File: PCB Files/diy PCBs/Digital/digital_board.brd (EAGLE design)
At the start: 50.8 x 58.4 mm, 18 parts

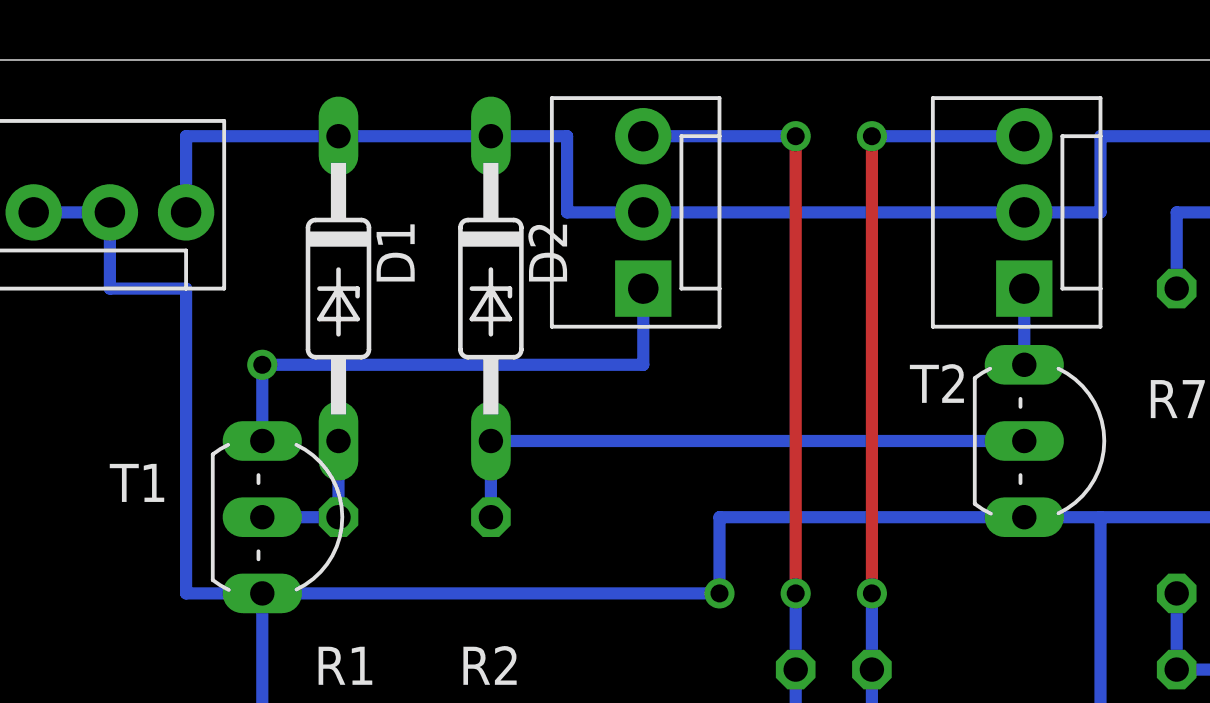
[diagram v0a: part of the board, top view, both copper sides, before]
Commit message: made fixed a small bug and changed diode parameters
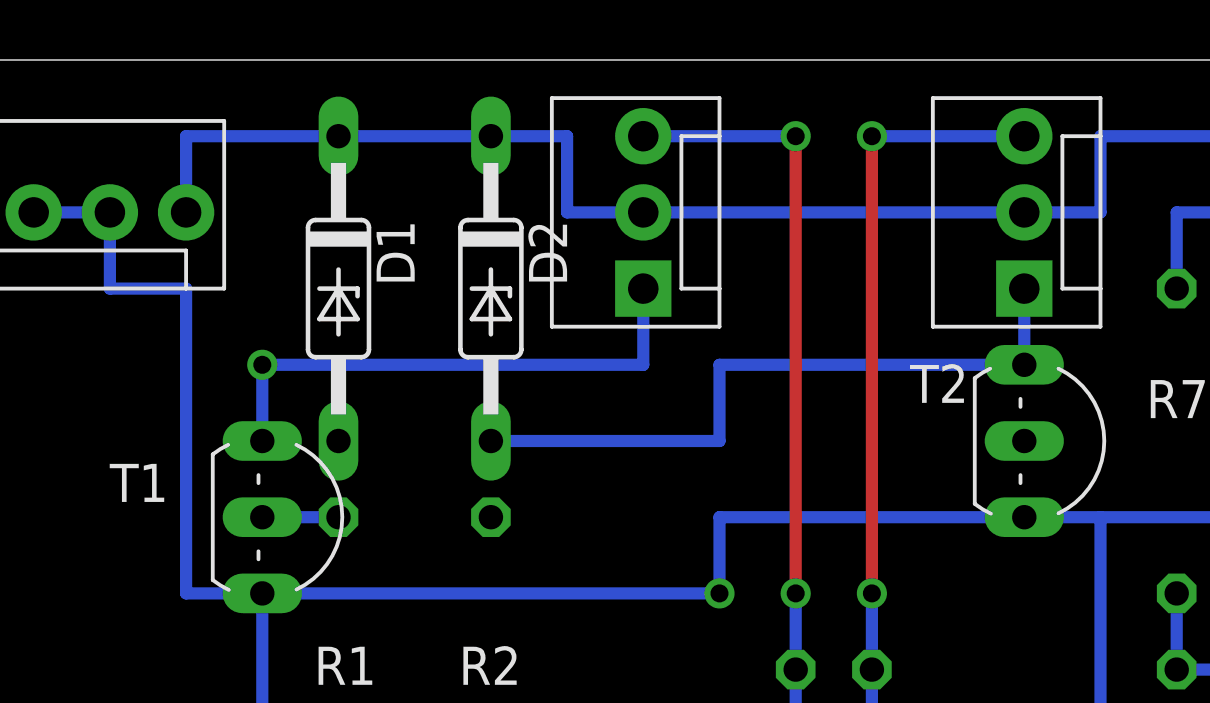
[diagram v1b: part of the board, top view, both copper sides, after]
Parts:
- D1, D2: value 1N821 -> 1N5819
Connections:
- removed net N$6: D2.A, R2.1, T2.B
- new net N$2: R2.1
- net N$3: now also D1.A
- net N$4: now also D2.A
- net N$5: no longer D1.A
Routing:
- net N$6: track 20.3 -> 0.00 mm
- net N$4: track 2.54 -> 22.9 mm
- net N$5: track 5.08 -> 2.54 mm
- net N$3: track 17.8 -> 20.3 mm
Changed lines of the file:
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@@
 <layer number="27" name="tValues" color="7" fill="1" visible="yes" active="yes"/>
 <layer number="28" name="bValues" color="7" fill="1" visible="yes" active="yes"/>
-<layer number="29" name="tStop" color="7" fill="3" visible="no" active="yes"/>
-<layer number="30" name="bStop" color="7" fill="6" visible="no" active="yes"/>
-<layer number="31" name="tCream" color="7" fill="4" visible="no" active="yes"/>
-<layer number="32" name="bCream" color="7" fill="5" visible="no" active="yes"/>
-<layer number="33" name="tFinish" color="6" fill="3" visible="no" active="yes"/>
-<layer number="34" name="bFinish" color="6" fill="6" visible="no" active="yes"/>
-<layer number="35" name="tGlue" color="7" fill="4" visible="no" active="yes"/>
-<layer number="36" name="bGlue" color="7" fill="5" visible="no" active="yes"/>
-<layer number="37" name="tTest" color="7" fill="1" visible="no" active="yes"/>
-<layer number="38" name="bTest" color="7" fill="1" visible="no" active="yes"/>
-<layer number="39" name="tKeepout" color="4" fill="11" visible="no" active="yes"/>
-<layer number="40" name="bKeepout" color="1" fill="11" visible="no" active="yes"/>
-<layer number="41" name="tRestrict" color="4" fill="10" visible="no" active="yes"/>
-<layer number="42" name="bRestrict" color="1" fill="10" visible="no" active="yes"/>
-<layer number="43" name="vRestrict" color="2" fill="10" visible="no" active="yes"/>
-<layer number="44" name="Drills" color="7" fill="1" visible="no" active="yes"/>
-<layer number="45" name="Holes" color="7" fill="1" visible="no" active="yes"/>
-<layer number="46" name="Milling" color="3" fill="1" visible="no" active="yes"/>
+<layer number="29" name="tStop" color="7" fill="3" visible="yes" active="yes"/>
+<layer number="30" name="bStop" color="7" fill="6" visible="yes" active="yes"/>
+<layer number="31" name="tCream" color="7" fill="4" visible="yes" active="yes"/>
+<layer number="32" name="bCream" color="7" fill="5" visible="yes" active="yes"/>
+<layer number="33" name="tFinish" color="6" fill="3" visible="yes" active="yes"/>
+<layer number="34" name="bFinish" color="6" fill="6" visible="yes" active="yes"/>
+<layer number="35" name="tGlue" color="7" fill="4" visible="yes" active="yes"/>
+<layer number="36" name="bGlue" color="7" fill="5" visible="yes" active="yes"/>
+<layer number="37" name="tTest" color="7" fill="1" visible="yes" active="yes"/>
+<layer number="38" name="bTest" color="7" fill="1" visible="yes" active="yes"/>
+<layer number="39" name="tKeepout" color="4" fill="11" visible="yes" active="yes"/>
+<layer number="40" name="bKeepout" color="1" fill="11" visible="yes" active="yes"/>
+<layer number="41" name="tRestrict" color="4" fill="10" visible="yes" active="yes"/>
+<layer number="42" name="bRestrict" color="1" fill="10" visible="yes" active="yes"/>
+<layer number="43" name="vRestrict" color="2" fill="10" visible="yes" active="yes"/>
+<layer number="44" name="Drills" color="7" fill="1" visible="yes" active="yes"/>
+<layer number="45" name="Holes" color="7" fill="1" visible="yes" active="yes"/>
+<layer number="46" name="Milling" color="3" fill="1" visible="yes" active="yes"/>
 <layer number="47" name="Measures" color="7" fill="1" visible="yes" active="yes"/>
 <layer number="48" name="Document" color="7" fill="1" visible="yes" active="yes"/>
@@
 <layer number="99" name="SpiceOrder" color="7" fill="1" visible="no" active="no"/>
 <layer number="100" name="Muster" color="7" fill="1" visible="no" active="no"/>
-<layer number="101" name="Patch_Top" color="12" fill="4" visible="no" active="yes"/>
+<layer number="101" name="Patch_Top" color="12" fill="4" visible="yes" active="yes"/>
 <layer number="102" name="Vscore" color="7" fill="1" visible="yes" active="yes"/>
 <layer number="103" name="tMap" color="7" fill="1" visible="yes" active="yes"/>
@@
 <layer number="112" name="tSilk" color="7" fill="1" visible="yes" active="yes"/>
 <layer number="113" name="IDFDebug" color="4" fill="1" visible="yes" active="yes"/>
-<layer number="116" name="Patch_BOT" color="9" fill="4" visible="no" active="yes"/>
+<layer number="116" name="Patch_BOT" color="9" fill="4" visible="yes" active="yes"/>
 <layer number="121" name="_tsilk" color="7" fill="1" visible="yes" active="yes"/>
 <layer number="122" name="_bsilk" color="7" fill="1" visible="yes" active="yes"/>
@@
 <layer number="155" name="FabDoc3" color="7" fill="1" visible="yes" active="yes"/>
 <layer number="199" name="Contour" color="7" fill="1" visible="yes" active="yes"/>
-<layer number="200" name="200bmp" color="1" fill="10" visible="no" active="yes"/>
-<layer number="201" name="201bmp" color="2" fill="10" visible="no" active="yes"/>
-<layer number="202" name="202bmp" color="3" fill="10" visible="no" active="yes"/>
-<layer number="203" name="203bmp" color="4" fill="10" visible="no" active="yes"/>
-<layer number="204" name="204bmp" color="5" fill="10" visible="no" active="yes"/>
-<layer number="205" name="205bmp" color="6" fill="10" visible="no" active="yes"/>
-<layer number="206" name="206bmp" color="7" fill="10" visible="no" active="yes"/>
-<layer number="207" name="207bmp" color="8" fill="10" visible="no" active="yes"/>
-<layer number="208" name="208bmp" color="9" fill="10" visible="no" active="yes"/>
+<layer number="200" name="200bmp" color="1" fill="10" visible="yes" active="yes"/>
+<layer number="201" name="201bmp" color="2" fill="10" visible="yes" active="yes"/>
+<layer number="202" name="202bmp" color="3" fill="10" visible="yes" active="yes"/>
+<layer number="203" name="203bmp" color="4" fill="10" visible="yes" active="yes"/>
+<layer number="204" name="204bmp" color="5" fill="10" visible="yes" active="yes"/>
+<layer number="205" name="205bmp" color="6" fill="10" visible="yes" active="yes"/>
+<layer number="206" name="206bmp" color="7" fill="10" visible="yes" active="yes"/>
+<layer number="207" name="207bmp" color="8" fill="10" visible="yes" active="yes"/>
+<layer number="208" name="208bmp" color="9" fill="10" visible="yes" active="yes"/>
 <layer number="209" name="209bmp" color="7" fill="1" visible="yes" active="yes"/>
 <layer number="210" name="210bmp" color="7" fill="1" visible="yes" active="yes"/>
@@
 <element name="PCB2" library="E14_Arduino_revB" package="ARDUINO_NANO" value="ARDUINO_NANO" x="1.27" y="1.27"/>
 <element name="JP7" library="SparkFun-Connectors" package="MOLEX-1X4" value="I²C" x="48.26" y="12.7" rot="MR270"/>
-<element name="D1" library="diode" package="DO35Z10" value="1N821" x="15.24" y="50.8" rot="R270"/>
-<element name="D2" library="diode" package="DO35Z10" value="1N821" x="20.32" y="50.8" rot="R270"/>
+<element name="D1" library="diode" package="DO35Z10" value="1N5819" x="15.24" y="50.8" rot="R270"/>
+<element name="D2" library="diode" package="DO35Z10" value="1N5819" x="20.32" y="50.8" rot="R270"/>
 </elements>
 <signals>
@@
 <contactref element="T1" pad="C"/>
 <wire x1="25.4" y1="50.8" x2="25.4" y2="48.26" width="0.4064" layer="16"/>
-<wire x1="25.4" y1="48.26" x2="12.7" y2="48.26" width="0.4064" layer="16"/>
+<wire x1="25.4" y1="48.26" x2="15.24" y2="48.26" width="0.4064" layer="16"/>
+<wire x1="15.24" y1="48.26" x2="12.7" y2="48.26" width="0.4064" layer="16"/>
 <wire x1="12.7" y1="48.26" x2="12.7" y2="45.72" width="0.4064" layer="16"/>
 <via x="12.7" y="48.26" extent="1-16" drill="0.6" shape="square"/>
+<contactref element="D1" pad="A"/>
+<wire x1="15.24" y1="45.72" x2="15.24" y2="48.26" width="0.4064" layer="16"/>
 </signal>
 <signal name="N$4">
@@
 <contactref element="T2" pad="C"/>
 <wire x1="38.1" y1="48.26" x2="38.1" y2="50.8" width="0.4064" layer="16"/>
+<contactref element="D2" pad="A"/>
+<wire x1="20.32" y1="45.72" x2="27.94" y2="45.72" width="0.4064" layer="16"/>
+<wire x1="27.94" y1="45.72" x2="27.94" y2="48.26" width="0.4064" layer="16"/>
+<wire x1="27.94" y1="48.26" x2="38.1" y2="48.26" width="0.4064" layer="16"/>
 </signal>
 <signal name="+12V">
@@
 <contactref element="JP5" pad="2"/>
 <contactref element="JP4" pad="2"/>
-<wire x1="20.32" y1="55.88" x2="22.86" y2="55.88" width="0.4064" layer="16"/>
 <wire x1="22.86" y1="55.88" x2="22.86" y2="53.34" width="0.4064" layer="16"/>
 <wire x1="22.86" y1="53.34" x2="25.4" y2="53.34" width="0.4064" layer="16"/>
@@
 <wire x1="40.64" y1="53.34" x2="40.64" y2="55.88" width="0.4064" layer="16"/>
 <wire x1="40.64" y1="55.88" x2="48.26" y2="55.88" width="0.4064" layer="16"/>
+<wire x1="10.16" y1="55.88" x2="10.16" y2="53.34" width="0.4064" layer="16"/>
 <contactref element="D1" pad="C"/>
 <contactref element="D2" pad="C"/>
+<wire x1="10.16" y1="55.88" x2="15.24" y2="55.88" width="0.4064" layer="16"/>
 <wire x1="15.24" y1="55.88" x2="20.32" y2="55.88" width="0.4064" layer="16"/>
-<wire x1="15.24" y1="55.88" x2="10.16" y2="55.88" width="0.4064" layer="16"/>
-<wire x1="10.16" y1="55.88" x2="10.16" y2="53.34" width="0.4064" layer="16"/>
+<wire x1="20.32" y1="55.88" x2="22.86" y2="55.88" width="0.4064" layer="16"/>
 </signal>
 <signal name="GND">
@@
 <contactref element="R1" pad="1"/>
 <wire x1="15.24" y1="43.18" x2="12.7" y2="43.18" width="0.4064" layer="16"/>
-<contactref element="D1" pad="A"/>
-<wire x1="15.24" y1="45.72" x2="15.24" y2="43.18" width="0.4064" layer="16"/>
-</signal>
-<signal name="N$6">
-<contactref element="T2" pad="B"/>
-<contactref element="R2" pad="1"/>
-<wire x1="20.32" y1="43.18" x2="20.32" y2="45.72" width="0.4064" layer="16"/>
-<wire x1="20.32" y1="45.72" x2="38.1" y2="45.72" width="0.4064" layer="16"/>
-<contactref element="D2" pad="A"/>
-<wire x1="20.32" y1="45.72" x2="20.32" y2="43.18" width="0" layer="19" extent="1-1"/>
 </signal>
 <signal name="N$8">
@@
 <wire x1="2.54" y1="22.86" x2="2.54" y2="53.34" width="0.4064" layer="16"/>
 </signal>
+<signal name="N$2">
+<contactref element="R2" pad="1"/>
+</signal>
 </signals>
